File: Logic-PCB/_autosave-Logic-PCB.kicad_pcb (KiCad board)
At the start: 2 copper layers, 118 parts, among them IC1 74LVC1G74DC-Q100H, IC10 SN74LVC1G11MDCKREP, IC11 SN74LVC1G11MDCKREP, IC12 SN74LVC1G97QDBVRQ1, IC13 SN74LVC1G97QDBVRQ1, IC14 TMUX1208QRSVRQ1, IC15 TMUX1208QRSVRQ1, IC16 TMUX1208QRSVRQ1, IC17 TMUX1208QRSVRQ1, IC18 TMUX1208QRSVRQ1, IC19 TMUX1208QRSVRQ1, IC2 74HC73D,653, IC20 TMUX1208QRSVRQ1, IC21 TMUX1208QRSVRQ1, IC22 TMUX1208QRSVRQ1, IC3 SN74LVC1G02DBVR, IC4 SN74LVC1G02DBVR, IC5 NCV4274AST33T3G, IC6 74AUP1T87GWH, IC7 74HC73D,653, IC8 TLC555QDRQ1, IC9 74HC73D,653, J1 CX70M-24P1, Q1 MMBT2222, Q10 MMBT2907A-7-F, Q11 MMBT2222, Q12 MMBT2222, Q13 MMBT2907A-7-F, Q2 MMBT2222, Q3 MMBT2222, Q4 MMBT2222, Q5 MMBT2907A-7-F, Q6 MMBT2907A-7-F, Q7 MMBT2222, Q8 MMBT2222, Q9 MMBT2907A-7-F, SW1 SW_Push, SW2 SW_Push, SW3 SW_Push, U1 74AHC1G86W5-7, U2 BAT-HLD-001-TR

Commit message: Decoupling Caps
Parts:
- moved D11 3.59 mm to (102.9, 56.3), turned to 90 degrees
- moved R28 3.08 mm to (98.8, 56.2), turned to 90 degrees
- moved R27 2.12 mm to (93.9, 56.2), turned to 90 degrees
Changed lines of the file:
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@@
   )
   (footprint "Resistor_SMD:R_0402_1005Metric" (layer "F.Cu")
-    (at 101.89 56.19)
+    (at 98.806 56.19 90)
     (descr "Resistor SMD 0402 (1005 Metric), square (rectangular) end terminal, IPC_7351 nominal, (Body size source: IPC-SM-782 page 72, https://www.pcb-3d.com/wordpress/wp-content/uploads/ipc-sm-782a_amendment_1_and_2.pdf), generated with kicad-footprint-generator")
     (tags "resistor")
@@
     (property "ki_keywords" "R res resistor")
     (attr smd)
-    (fp_text reference "R28" (at 0 -1.17) (layer "F.SilkS")
+    (fp_text reference "R28" (at 0 -1.17 90) (layer "F.SilkS")
         (effects (font (size 1 1) (thickness 0.15)))
     )
-    (fp_text value "100" (at 0 1.17) (layer "F.Fab")
+    (fp_text value "100" (at 0 1.17 90) (layer "F.Fab")
         (effects (font (size 1 1) (thickness 0.15)))
     )
-    (fp_text user "${REFERENCE}" (at 0 0) (layer "F.Fab")
+    (fp_text user "${REFERENCE}" (at 0 0 90) (layer "F.Fab")
         (effects (font (size 0.26 0.26) (thickness 0.04)))
     )
@@
     (fp_line (start 0.525 0.27) (end -0.525 0.27)
       (stroke (width 0.1) (type solid)) (layer "F.Fab"))
-    (pad "1" smd roundrect (at -0.51 0) (size 0.54 0.64) (layers "F.Cu" "F.Paste" "F.Mask") (roundrect_rratio 0.25)
+    (pad "1" smd roundrect (at -0.51 0 90) (size 0.54 0.64) (layers "F.Cu" "F.Paste" "F.Mask") (roundrect_rratio 0.25)
       (net 1 "+3V0") (pintype "passive"))
-    (pad "2" smd roundrect (at 0.51 0) (size 0.54 0.64) (layers "F.Cu" "F.Paste" "F.Mask") (roundrect_rratio 0.25)
+    (pad "2" smd roundrect (at 0.51 0 90) (size 0.54 0.64) (layers "F.Cu" "F.Paste" "F.Mask") (roundrect_rratio 0.25)
       (net 17 "Net-(D11-A)") (pintype "passive"))
     (model "${KICAD6_3DMODEL_DIR}/Resistor_SMD.3dshapes/R_0402_1005Metric.wrl"
@@
   )
   (footprint "LED_SMD:LED_0402_1005Metric" (layer "F.Cu")
-    (at 106.46 56.19)
+    (at 102.87 56.261 90)
     (descr "LED SMD 0402 (1005 Metric), square (rectangular) end terminal, IPC_7351 nominal, (Body size source: http://www.tortai-tech.com/upload/download/2011102023233369053.pdf), generated with kicad-footprint-generator")
     (tags "LED")
@@
     (property "ki_keywords" "LED diode")
     (attr smd)
-    (fp_text reference "D11" (at 0 -1.17) (layer "F.SilkS")
+    (fp_text reference "D11" (at 0 -1.17 90) (layer "F.SilkS")
         (effects (font (size 1 1) (thickness 0.15)))
     )
-    (fp_text value "LED" (at 0 1.17) (layer "F.Fab")
+    (fp_text value "LED" (at 0 1.17 90) (layer "F.Fab")
         (effects (font (size 1 1) (thickness 0.15)))
     )
-    (fp_text user "${REFERENCE}" (at 0 0) (layer "F.Fab")
+    (fp_text user "${REFERENCE}" (at 0 0 90) (layer "F.Fab")
         (effects (font (size 0.25 0.25) (thickness 0.04)))
     )
@@
     (fp_line (start 0.5 0.25) (end -0.5 0.25)
       (stroke (width 0.1) (type solid)) (layer "F.Fab"))
-    (pad "1" smd roundrect (at -0.485 0) (size 0.59 0.64) (layers "F.Cu" "F.Paste" "F.Mask") (roundrect_rratio 0.25)
+    (pad "1" smd roundrect (at -0.485 0 90) (size 0.59 0.64) (layers "F.Cu" "F.Paste" "F.Mask") (roundrect_rratio 0.25)
       (net 16 "Net-(D11-K)") (pinfunction "K") (pintype "passive"))
-    (pad "2" smd roundrect (at 0.485 0) (size 0.59 0.64) (layers "F.Cu" "F.Paste" "F.Mask") (roundrect_rratio 0.25)
+    (pad "2" smd roundrect (at 0.485 0 90) (size 0.59 0.64) (layers "F.Cu" "F.Paste" "F.Mask") (roundrect_rratio 0.25)
       (net 17 "Net-(D11-A)") (pinfunction "A") (pintype "passive"))
     (model "${KICAD6_3DMODEL_DIR}/LED_SMD.3dshapes/LED_0402_1005Metric.wrl"
@@
   )
   (footprint "Resistor_SMD:R_0402_1005Metric" (layer "F.Cu")
-    (at 91.73 56.19)
+    (at 93.853 56.19 90)
     (descr "Resistor SMD 0402 (1005 Metric), square (rectangular) end terminal, IPC_7351 nominal, (Body size source: IPC-SM-782 page 72, https://www.pcb-3d.com/wordpress/wp-content/uploads/ipc-sm-782a_amendment_1_and_2.pdf), generated with kicad-footprint-generator")
     (tags "resistor")
@@
     (property "ki_keywords" "R res resistor")
     (attr smd)
-    (fp_text reference "R27" (at 0 -1.17) (layer "F.SilkS")
+    (fp_text reference "R27" (at 0 -1.17 90) (layer "F.SilkS")
         (effects (font (size 1 1) (thickness 0.15)))
     )
-    (fp_text value "5.6k" (at 0 1.17) (layer "F.Fab")
+    (fp_text value "5.6k" (at 0 1.17 90) (layer "F.Fab")
         (effects (font (size 1 1) (thickness 0.15)))
     )
-    (fp_text user "${REFERENCE}" (at 0 0) (layer "F.Fab")
+    (fp_text user "${REFERENCE}" (at 0 0 90) (layer "F.Fab")
         (effects (font (size 0.26 0.26) (thickness 0.04)))
     )
@@
     (fp_line (start 0.525 0.27) (end -0.525 0.27)
       (stroke (width 0.1) (type solid)) (layer "F.Fab"))
-    (pad "1" smd roundrect (at -0.51 0) (size 0.54 0.64) (layers "F.Cu" "F.Paste" "F.Mask") (roundrect_rratio 0.25)
+    (pad "1" smd roundrect (at -0.51 0 90) (size 0.54 0.64) (layers "F.Cu" "F.Paste" "F.Mask") (roundrect_rratio 0.25)
       (net 37 "Button A") (pintype "passive"))
-    (pad "2" smd roundrect (at 0.51 0) (size 0.54 0.64) (layers "F.Cu" "F.Paste" "F.Mask") (roundrect_rratio 0.25)
+    (pad "2" smd roundrect (at 0.51 0 90) (size 0.54 0.64) (layers "F.Cu" "F.Paste" "F.Mask") (roundrect_rratio 0.25)
       (net 128 "Net-(Q13-Pad1)") (pintype "passive"))
     (model "${KICAD6_3DMODEL_DIR}/Resistor_SMD.3dshapes/R_0402_1005Metric.wrl"

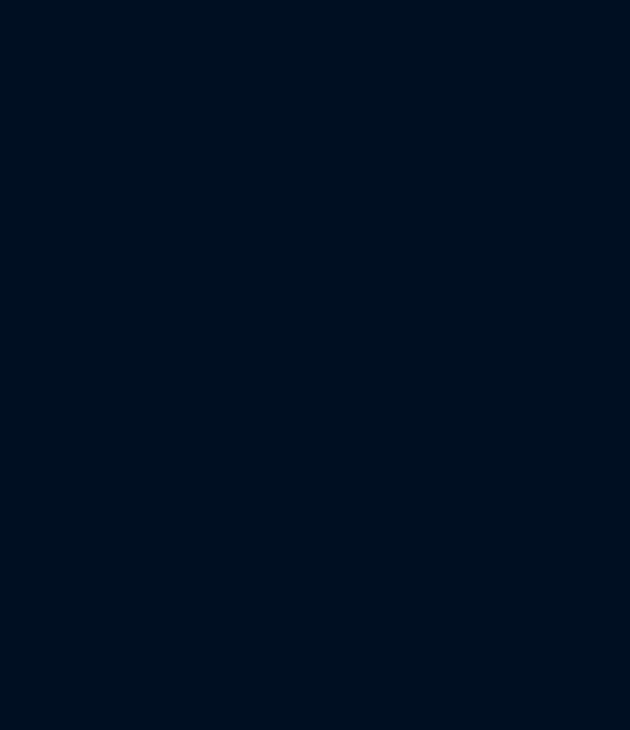
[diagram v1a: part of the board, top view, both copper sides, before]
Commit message: Removing pulldown resistors
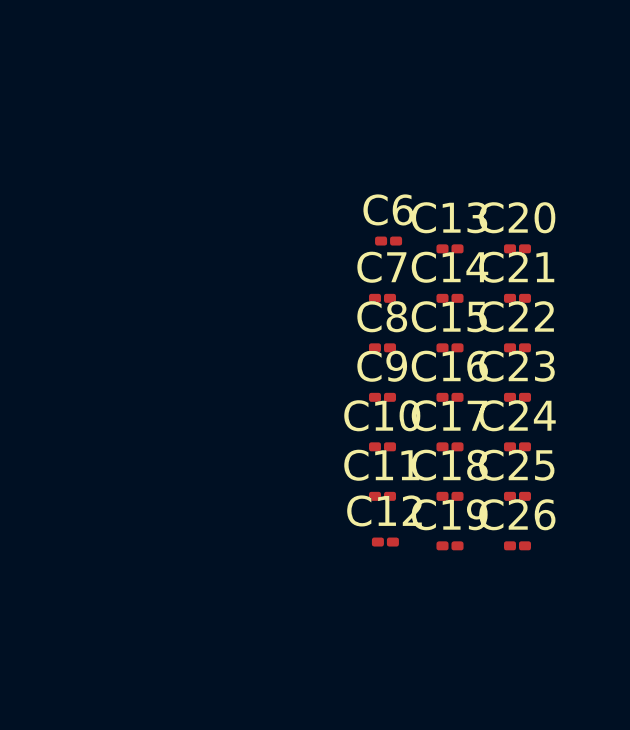
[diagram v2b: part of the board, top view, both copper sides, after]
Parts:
- added C10: .1u, Capacitor_SMD:C_01005_0402Metric, F.Cu at (173.4, 91.1)
- added C11: .1u, Capacitor_SMD:C_01005_0402Metric, F.Cu at (173.4, 92.7)
- added C12: .1u, Capacitor_SMD:C_01005_0402Metric, F.Cu at (173.5, 94.2)
- added C13: .1u, Capacitor_SMD:C_01005_0402Metric, F.Cu at (175.7, 84.5)
- added C14: .1u, Capacitor_SMD:C_01005_0402Metric, F.Cu at (175.7, 86.1)
- added C15: .1u, Capacitor_SMD:C_01005_0402Metric, F.Cu at (175.7, 87.8)
- added C16: .1u, Capacitor_SMD:C_01005_0402Metric, F.Cu at (175.7, 89.4)
- added C17: .1u, Capacitor_SMD:C_01005_0402Metric, F.Cu at (175.7, 91.1)
- added C18: .1u, Capacitor_SMD:C_01005_0402Metric, F.Cu at (175.7, 92.7)
- added C19: .1u, Capacitor_SMD:C_01005_0402Metric, F.Cu at (175.7, 94.4)
- added C20: .1u, Capacitor_SMD:C_01005_0402Metric, F.Cu at (177.9, 84.5)
- added C21: .1u, Capacitor_SMD:C_01005_0402Metric, F.Cu at (177.9, 86.1)
- added C22: .1u, Capacitor_SMD:C_01005_0402Metric, F.Cu at (177.9, 87.8)
- added C23: .1u, Capacitor_SMD:C_01005_0402Metric, F.Cu at (177.9, 89.4)
- added C24: .1u, Capacitor_SMD:C_01005_0402Metric, F.Cu at (177.9, 91.1)
- added C25: .1u, Capacitor_SMD:C_01005_0402Metric, F.Cu at (177.9, 92.7)
- added C26: .1u, Capacitor_SMD:C_01005_0402Metric, F.Cu at (177.9, 94.4)
- added C6: .1u, Capacitor_SMD:C_01005_0402Metric, F.Cu at (173.6, 84.2)
- added C7: .1u, Capacitor_SMD:C_01005_0402Metric, F.Cu at (173.4, 86.1)
- added C8: .1u, Capacitor_SMD:C_01005_0402Metric, F.Cu at (173.4, 87.8)
- added C9: .1u, Capacitor_SMD:C_01005_0402Metric, F.Cu at (173.4, 89.4)
